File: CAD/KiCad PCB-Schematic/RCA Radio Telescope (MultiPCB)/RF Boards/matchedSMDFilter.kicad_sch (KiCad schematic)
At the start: 3 parts, among them J11 ANT, J15 ANT, U15 BPF-A1340+

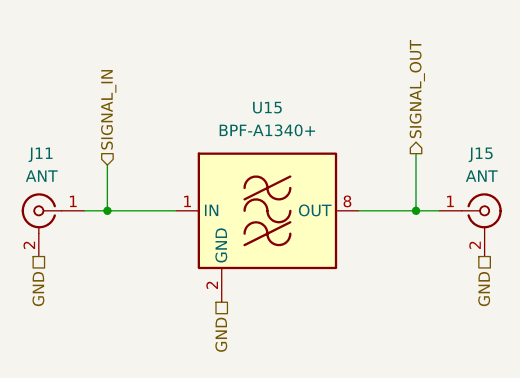
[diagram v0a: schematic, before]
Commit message: RF Boards Redo (WIP)
- Overhauling current RF boards to keep 4 RF boards in total
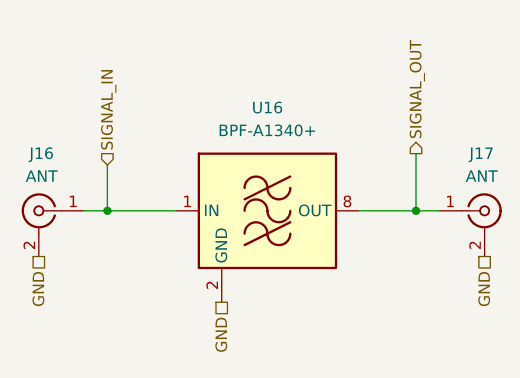
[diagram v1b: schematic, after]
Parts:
- removed J11, J15: ANT, Library:CONN_142-0711-821_CIN, symbol Connector:Conn_Coaxial
- removed U15: BPF-A1340+, RF_Mini-Circuits:Mini-Circuits_HQ1157, symbol RF_Filter:BPF-A355
- added J16, J17: ANT, Library:CONN_142-0711-821_CIN, symbol Connector:Conn_Coaxial
- added U16: BPF-A1340+, RF_Mini-Circuits:Mini-Circuits_HQ1157, symbol RF_Filter:BPF-A355
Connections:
- net GND: now also J16.2 (Ext), J17.2 (Ext), U16.10 (GND), U16.11 (GND), U16.12 (GND), U16.13 (GND), U16.14 (GND), U16.2 (GND), U16.3 (GND), U16.4 (GND), U16.5 (GND), U16.6 (GND), U16.7 (GND), U16.9 (GND)
- net SIGNAL_IN: now also J16.1 (In), U16.1 (IN)
- net SIGNAL_OUT: now also J17.1 (In), U16.8 (OUT)
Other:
- title: SMDFilter -> Matched SMD Filter
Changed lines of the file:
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@@
 	(paper "A5")
 	(title_block
-		(title "SMDFilter")
+		(title "Matched SMD Filter")
 		(date "2025-04-08")
 		(rev "v1.0")
@@
 	(hierarchical_label "GND"
 		(shape passive)
+		(at 85.09 60.96 270)
+		(effects
+			(font
+				(size 1.27 1.27)
+			)
+			(justify right)
+		)
+	)
+	(hierarchical_label "GND"
+		(shape passive)
+		(at 55.88 66.04 270)
+		(effects
+			(font
+				(size 1.27 1.27)
+			)
+			(justify right)
+		)
+	)
+	(hierarchical_label "GND"
+		(shape passive)
 		(at 35.56 60.96 270)
 		(effects
@@
 			)
 			(justify right)
+		)
+	)
+	(hierarchical_label "SIGNAL_IN"
+		(shape input)
+		(at 43.18 50.8 90)
+		(effects
+			(font
+				(size 1.27 1.27)
+			)
+			(justify left)
 		)
 	)
@@
 			)
 			(justify left)
-		)
-	)
-	(hierarchical_label "GND"
-		(shape passive)
-		(at 55.88 66.04 270)
-		(effects
-			(font
-				(size 1.27 1.27)
-			)
-			(justify right)
-		)
-	)
-	(hierarchical_label "SIGNAL_IN"
-		(shape input)
-		(at 43.18 50.8 90)
-		(effects
-			(font
-				(size 1.27 1.27)
-			)
-			(justify left)
-		)
-	)
-	(hierarchical_label "GND"
-		(shape passive)
-		(at 85.09 60.96 270)
-		(effects
-			(font
-				(size 1.27 1.27)
-			)
-			(justify right)
 		)
 	)
@@
 		(on_board yes)
 		(dnp no)
-		(property "Reference" "J15"
+		(property "Reference" "J17"
 			(at 84.7726 49.53 0)
 			(effects
@@
 		(instances
 			(project "RCA Radio Telescope"
-				(path "/1630c5ee-b70a-455e-85ba-86a73955b8fd/b1bd03bb-513c-4075-8ea8-0ed535b26dec"
-					(reference "J15")
+				(path "/1630c5ee-b70a-455e-85ba-86a73955b8fd/d56a2cda-b123-4fba-9e43-f9d7e5baedc8"
+					(reference "J17")
 					(unit 1)
 				)
-				(path "/1630c5ee-b70a-455e-85ba-86a73955b8fd/b4999127-d4ab-471a-8016-d4958c63707b"
-					(reference "J21")
-					(unit 1)
-				)
+			)
+		)
+	)
+	(symbol
+		(lib_id "RF_Filter:BPF-A355")
+		(at 60.96 55.88 0)
+		(unit 1)
+		(exclude_from_sim no)
+		(in_bom yes)
+		(on_board yes)
+		(dnp no)
+		(fields_autoplaced yes)
+		(property "Reference" "U16"
+			(at 60.96 44.45 0)
+			(effects
+				(font
+					(size 1.27 1.27)
+				)
+			)
+		)
+		(property "Value" "BPF-A1340+"
+			(at 60.96 46.99 0)
+			(effects
+				(font
+					(size 1.27 1.27)
+				)
+			)
+		)
+		(property "Footprint" "RF_Mini-Circuits:Mini-Circuits_HQ1157"
+			(at 60.96 68.58 0)
+			(effects
+				(font
+					(size 1.27 1.27)
+				)
+				(hide yes)
+			)
+		)
+		(property "Datasheet" "https://www.minicircuits.com/pdfs/BPF-A355+.pdf"
+			(at 60.96 53.34 0)
+			(effects
+				(font
+					(size 1.27 1.27)
+				)
+				(hide yes)
+			)
+		)
+		(property "Description" "Bandpass Filter, 310 to 400 MHz, 50 Ohm, Mini-Circuits HQ1157"
+			(at 60.96 55.88 0)
+			(effects
+				(font
+					(size 1.27 1.27)
+				)
+				(hide yes)
+			)
+		)
+		(pin "3"
+		)
+		(pin "9"
+		)
+		(pin "12"
+		)
+		(pin "13"
+		)
+		(pin "6"
+		)
+		(pin "4"
+		)
+		(pin "10"
+		)
+		(pin "7"
+		)
+		(pin "11"
+		)
+		(pin "14"
+		)
+		(pin "1"
+		)
+		(pin "5"
+		)
+		(pin "8"
+		)
+		(pin "2"
+		)
+		(instances
+			(project "RCA Radio Telescope"
 				(path "/1630c5ee-b70a-455e-85ba-86a73955b8fd/d56a2cda-b123-4fba-9e43-f9d7e5baedc8"
-					(reference "J19")
+					(reference "U16")
 					(unit 1)
 				)
@@
 		(dnp no)
 		(fields_autoplaced yes)
-		(property "Reference" "J11"
+		(property "Reference" "J16"
 			(at 35.8774 49.53 0)
 			(effects
@@
 		(instances
 			(project "RCA Radio Telescope"
-				(path "/1630c5ee-b70a-455e-85ba-86a73955b8fd/b1bd03bb-513c-4075-8ea8-0ed535b26dec"
-					(reference "J11")
+				(path "/1630c5ee-b70a-455e-85ba-86a73955b8fd/d56a2cda-b123-4fba-9e43-f9d7e5baedc8"
+					(reference "J16")
 					(unit 1)
 				)
-				(path "/1630c5ee-b70a-455e-85ba-86a73955b8fd/b4999127-d4ab-471a-8016-d4958c63707b"
-					(reference "J20")
-					(unit 1)
-				)
-				(path "/1630c5ee-b70a-455e-85ba-86a73955b8fd/d56a2cda-b123-4fba-9e43-f9d7e5baedc8"
-					(reference "J18")
-					(unit 1)
-				)
-			)
-		)
-	)
-	(symbol
-		(lib_id "RF_Filter:BPF-A355")
-		(at 60.96 55.88 0)
-		(unit 1)
-		(exclude_from_sim no)
-		(in_bom yes)
-		(on_board yes)
-		(dnp no)
-		(fields_autoplaced yes)
-		(property "Reference" "U15"
-			(at 60.96 44.45 0)
-			(effects
-				(font
-					(size 1.27 1.27)
-				)
-			)
-		)
-		(property "Value" "BPF-A1340+"
-			(at 60.96 46.99 0)
-			(effects
-				(font
-					(size 1.27 1.27)
-				)
-			)
-		)
-		(property "Footprint" "RF_Mini-Circuits:Mini-Circuits_HQ1157"
-			(at 60.96 68.58 0)
-			(effects
-				(font
-					(size 1.27 1.27)
-				)
-				(hide yes)
-			)
-		)
-		(property "Datasheet" "https://www.minicircuits.com/pdfs/BPF-A355+.pdf"
-			(at 60.96 53.34 0)
-			(effects
-				(font
-					(size 1.27 1.27)
-				)
-				(hide yes)
-			)
-		)
-		(property "Description" "Bandpass Filter, 310 to 400 MHz, 50 Ohm, Mini-Circuits HQ1157"
-			(at 60.96 55.88 0)
-			(effects
-				(font
-					(size 1.27 1.27)
-				)
-				(hide yes)
-			)
-		)
-		(pin "3"
-		)
-		(pin "9"
-		)
-		(pin "12"
-		)
-		(pin "13"
-		)
-		(pin "6"
-		)
-		(pin "4"
-		)
-		(pin "10"
-		)
-		(pin "7"
-		)
-		(pin "11"
-		)
-		(pin "14"
-		)
-		(pin "1"
-		)
-		(pin "5"
-		)
-		(pin "8"
-		)
-		(pin "2"
-		)
-		(instances
-			(project "RCA Radio Telescope"
-				(path "/1630c5ee-b70a-455e-85ba-86a73955b8fd/b1bd03bb-513c-4075-8ea8-0ed535b26dec"
-					(reference "U15")
-					(unit 1)
-				)
-				(path "/1630c5ee-b70a-455e-85ba-86a73955b8fd/b4999127-d4ab-471a-8016-d4958c63707b"
-					(reference "U17")
-					(unit 1)
-				)
-				(path "/1630c5ee-b70a-455e-85ba-86a73955b8fd/d56a2cda-b123-4fba-9e43-f9d7e5baedc8"
-					(reference "U17")
-					(unit 1)
-				)
